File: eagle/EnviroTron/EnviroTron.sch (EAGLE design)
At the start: 14 parts

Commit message: Cleaned up small layout details
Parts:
- removed U$2: WEMOS-D1-MINI, Enviro:WEMOS-D1-MINI
- added COMMS: WEMOS-D1-MINI, EnviroTron:WEMOS-D1-MINI
- LIGHT: device Enviro:LTR-329 -> EnviroTron:LTR-329
- MOTION: device Enviro:PIR -> EnviroTron:PIR
- PRES: device Enviro:MS5607 -> EnviroTron:MS5607
- TEMP: device Enviro:SHT21 -> EnviroTron:SHT21
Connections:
- net 3V3: now also COMMS.3V3; no longer U$2.3V3
- net GND: now also COMMS.GND; no longer U$2.GND
- net PIROUT: now also COMMS.D0; no longer U$2.D0
- net SCL: now also COMMS.D1; no longer U$2.D1
- net SDA: now also COMMS.D2; no longer U$2.D2
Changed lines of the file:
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@@
 <part name="C3" library="rcl" deviceset="C-US" device="C0805" value="100n"/>
 <part name="C4" library="rcl" deviceset="C-US" device="C0805" value="100n"/>
-<part name="LIGHT" library="Enviro" deviceset="LTR-329" device=""/>
-<part name="PRES" library="Enviro" deviceset="MS5607" device=""/>
+<part name="LIGHT" library="EnviroTron" deviceset="LTR-329" device=""/>
+<part name="PRES" library="EnviroTron" deviceset="MS5607" device=""/>
 <part name="R1" library="rcl" deviceset="R-US_" device="R0805" value="10k"/>
 <part name="R2" library="rcl" deviceset="R-US_" device="R0805" value="10k"/>
 <part name="C5" library="rcl" deviceset="C-US" device="C0805" value="1u"/>
 <part name="C6" library="rcl" deviceset="C-US" device="C0805" value="10u"/>
-<part name="MOTION" library="Enviro" deviceset="PIR" device=""/>
+<part name="MOTION" library="EnviroTron" deviceset="PIR" device=""/>
 <part name="R3" library="rcl" deviceset="R-US_" device="R0805" value="10k"/>
-<part name="TEMP" library="Enviro" deviceset="SHT21" device=""/>
-<part name="U$2" library="Enviro" deviceset="WEMOS-D1-MINI" device=""/>
+<part name="TEMP" library="EnviroTron" deviceset="SHT21" device=""/>
+<part name="COMMS" library="EnviroTron" deviceset="WEMOS-D1-MINI" device=""/>
 </parts>
 <sheets>
@@
 <instance part="R3" gate="G$1" x="88.9" y="99.06"/>
 <instance part="TEMP" gate="G$1" x="68.58" y="25.4"/>
-<instance part="U$2" gate="G$1" x="17.78" y="17.78"/>
+<instance part="COMMS" gate="G$1" x="17.78" y="17.78"/>
 </instances>
 <busses>
@@
 <wire x1="7.62" y1="22.86" x2="5.08" y2="22.86" width="0.1524" layer="91"/>
 <label x="5.08" y="22.86" size="1.524" layer="95" rot="R180" xref="yes"/>
-<pinref part="U$2" gate="G$1" pin="D2"/>
+<pinref part="COMMS" gate="G$1" pin="D2"/>
 </segment>
 <segment>
@@
 <wire x1="7.62" y1="25.4" x2="5.08" y2="25.4" width="0.1524" layer="91"/>
 <label x="5.08" y="25.4" size="1.524" layer="95" rot="R180" xref="yes"/>
-<pinref part="U$2" gate="G$1" pin="D1"/>
+<pinref part="COMMS" gate="G$1" pin="D1"/>
 </segment>
 <segment>
@@
 <wire x1="27.94" y1="22.86" x2="30.48" y2="22.86" width="0.1524" layer="91"/>
 <label x="30.48" y="22.86" size="1.524" layer="95" xref="yes"/>
-<pinref part="U$2" gate="G$1" pin="3V3"/>
+<pinref part="COMMS" gate="G$1" pin="3V3"/>
 </segment>
 <segment>
@@
 <wire x1="27.94" y1="15.24" x2="30.48" y2="15.24" width="0.1524" layer="91"/>
 <label x="30.48" y="15.24" size="1.524" layer="95" xref="yes"/>
-<pinref part="U$2" gate="G$1" pin="GND"/>
+<pinref part="COMMS" gate="G$1" pin="GND"/>
 </segment>
 <segment>
@@
 <wire x1="7.62" y1="27.94" x2="5.08" y2="27.94" width="0.1524" layer="91"/>
 <label x="5.08" y="27.94" size="1.524" layer="95" rot="R180" xref="yes"/>
-<pinref part="U$2" gate="G$1" pin="D0"/>
-</segment>
-</net>
+<pinref part="COMMS" gate="G$1" pin="D0"/>
+</segment>
+</net>

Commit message: Fixed floating CSB pin on MS5607 chip
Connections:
- net GND: now also PRES.CSB
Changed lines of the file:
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@@
 <label x="96.52" y="99.06" size="1.524" layer="95" xref="yes"/>
+</segment>
+<segment>
+<pinref part="PRES" gate="G$1" pin="CSB"/>
+<wire x1="81.28" y1="78.74" x2="83.82" y2="78.74" width="0.1524" layer="91"/>
+<label x="83.82" y="78.74" size="1.524" layer="95" xref="yes"/>
 </segment>
 </net>

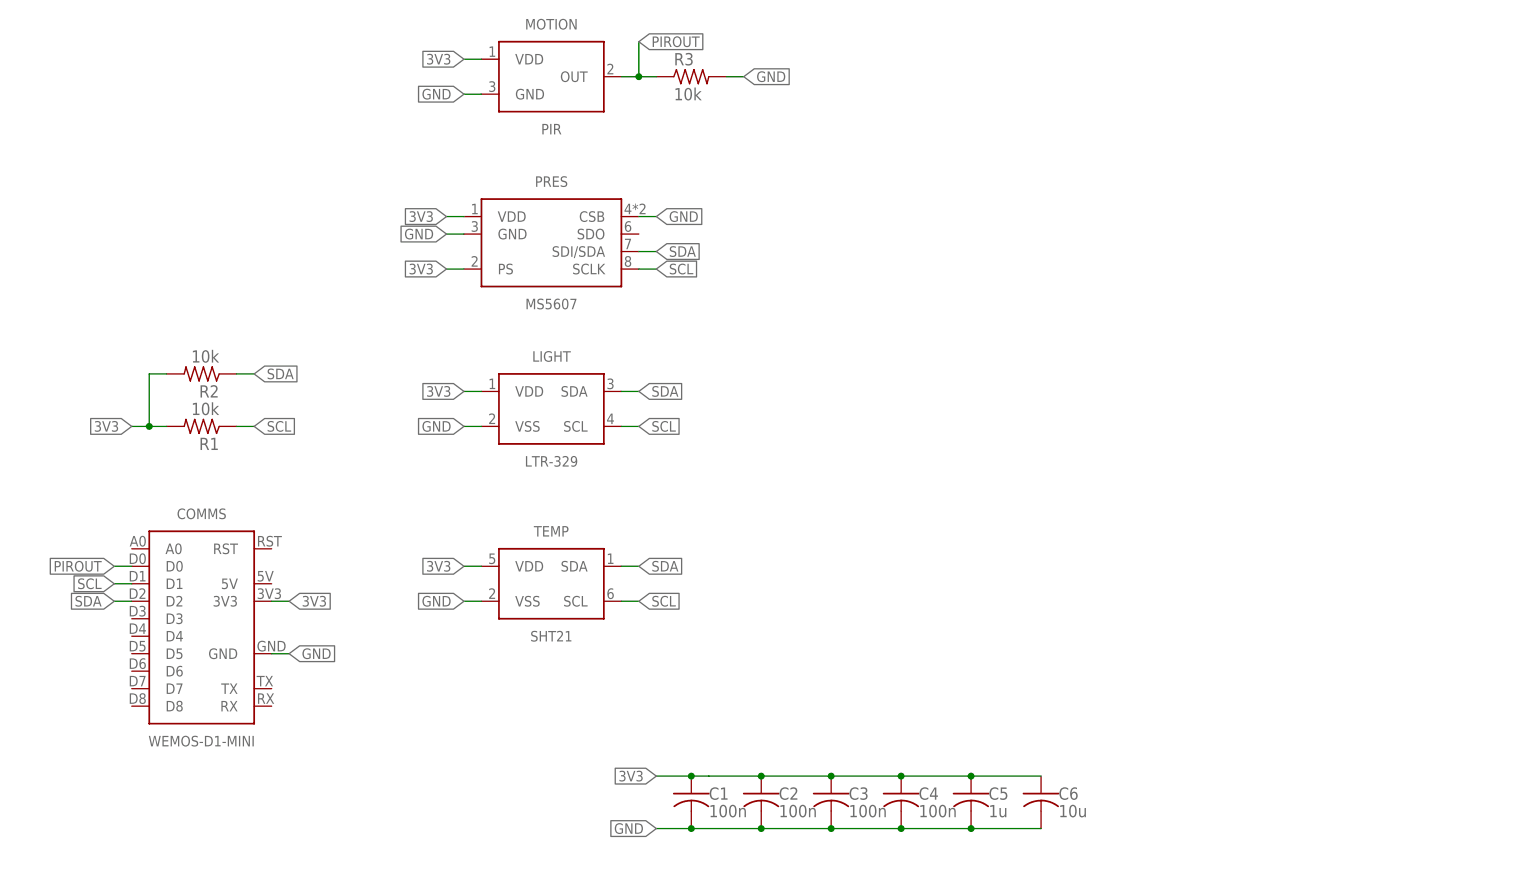
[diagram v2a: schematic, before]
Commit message: Added sound sensor to EnviroTron board. Swapped to better Pressure sensor.
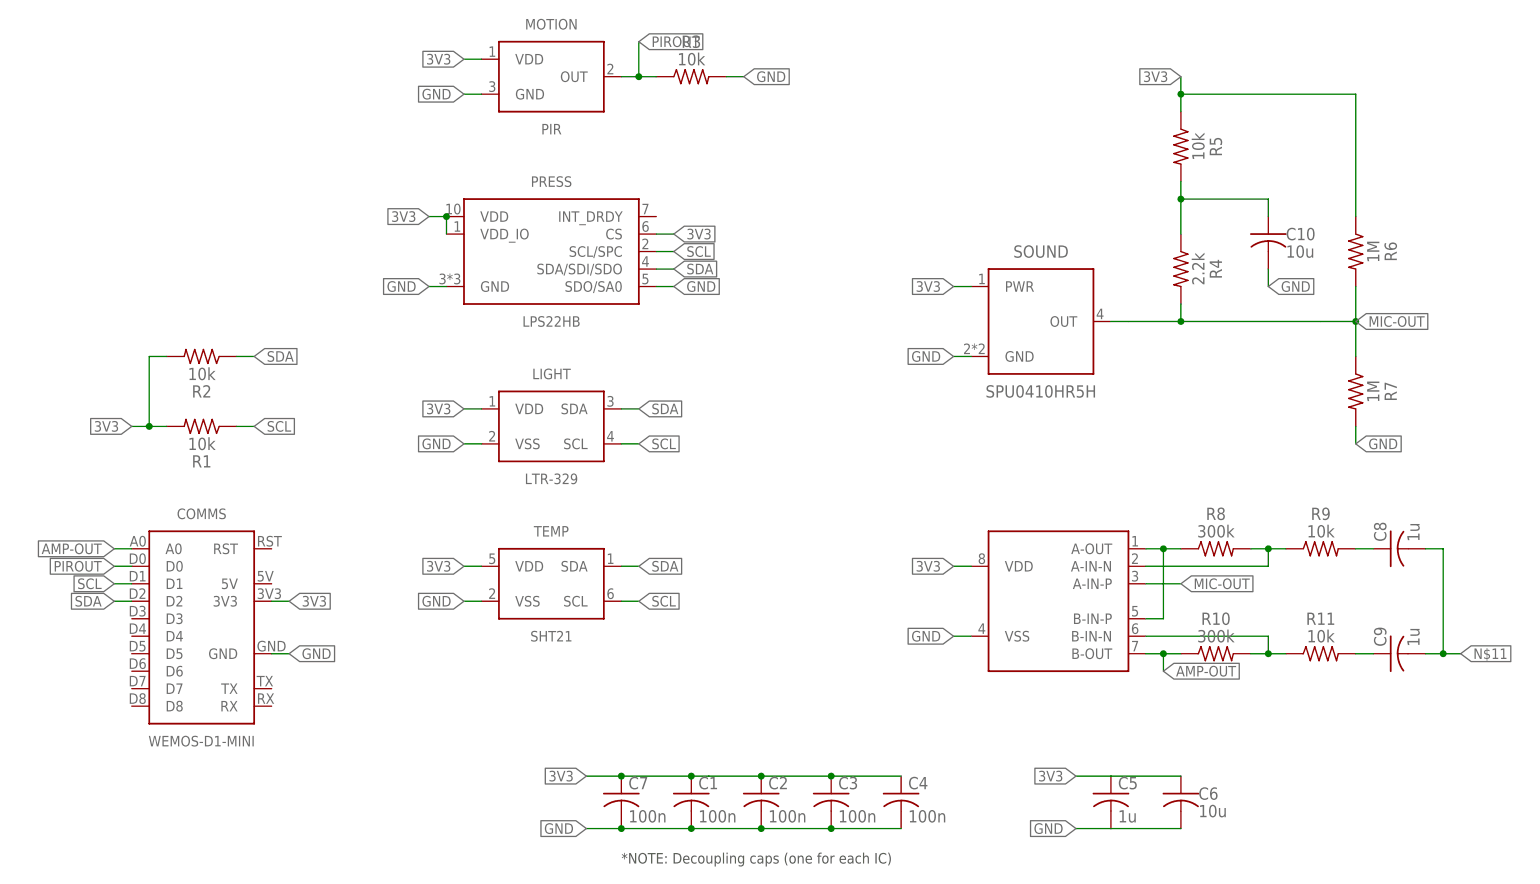
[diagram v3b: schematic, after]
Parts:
- removed PRES: MS5607, EnviroTron:MS5607
- added C10: 10u, rcl:C-USC0805
- added C7: 100n, SmslsTron-1:C-USC0603
- added C8, C9: 1u, SmslsTron-1:C-USC0603
- added PRESS: LPS22HB, EnviroTron:LPS22HB
- added R10, R8: 300k, SmslsTron-1:R-US_R0603
- added R11, R5, R9: 10k, SmslsTron-1:R-US_R0603
- added R4: 2.2k, SmslsTron-1:R-US_R0603
- added R6, R7: 1M, SmslsTron-1:R-US_R0603
- added SOUND: SPU0410HR5H, EnviroTron:SPU0410HR5H
- added U$1: MCP6002, EnviroTron:MCP6002
- C1, C2, C3, C4, C5: device rcl:C-USC0805 -> SmslsTron-1:C-USC0603
- R1, R2, R3: device rcl:R-US_R0805 -> SmslsTron-1:R-US_R0603
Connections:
- new net AMP-OUT: COMMS.A0, R10.1, U$1.B-OUT
- new net MIC-OUT: R4.2, R6.2, R7.1, SOUND.OUT, U$1.A-IN-P
- new net N$10: C9.1, R11.2
- new net N$11: C8.2, C9.2
- new net N$2: R8.1, U$1.A-OUT, U$1.B-IN-P
- new net N$3: C5.1, C6.1
- new net N$4: C5.2, C6.2
- new net N$5: C10.1, R4.1, R5.2
- new net N$6: R8.2, R9.1, U$1.A-IN-N
- new net N$7: C8.1, R9.2
- new net N$9: R10.2, R11.1, U$1.B-IN-N
- net 3V3: now also C7.1, PRESS.CS, PRESS.VDD, PRESS.VDD_IO, R5.1, R6.1, SOUND.PWR; no longer C5.1, C6.1, PRES.PS, PRES.VDD
- net GND: now also C10.2, C7.2, PRESS.GND, PRESS.SDO/SA0, R7.2, SOUND.GND; no longer C5.2, C6.2, PRES.CSB, PRES.GND
- net SCL: now also PRESS.SCL/SPC; no longer PRES.SCLK
- net SDA: now also PRESS.SDA/SDI/SDO; no longer PRES.SDI/SDA
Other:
- note added: "*NOTE: Decoupling caps (one for each IC)"
- moved on the sheet: C6, LIGHT, R2

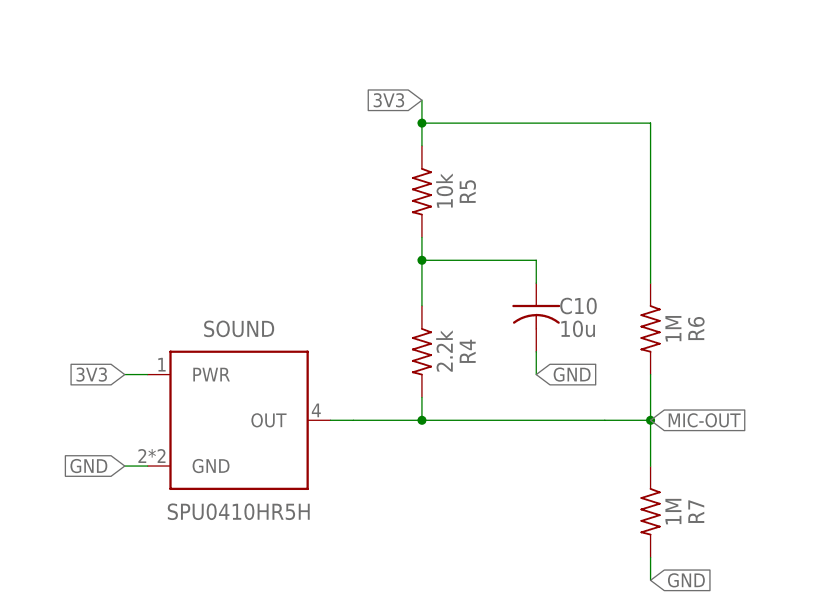
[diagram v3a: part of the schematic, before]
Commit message: Added DC blocking cap to mic pre-amp circuit.
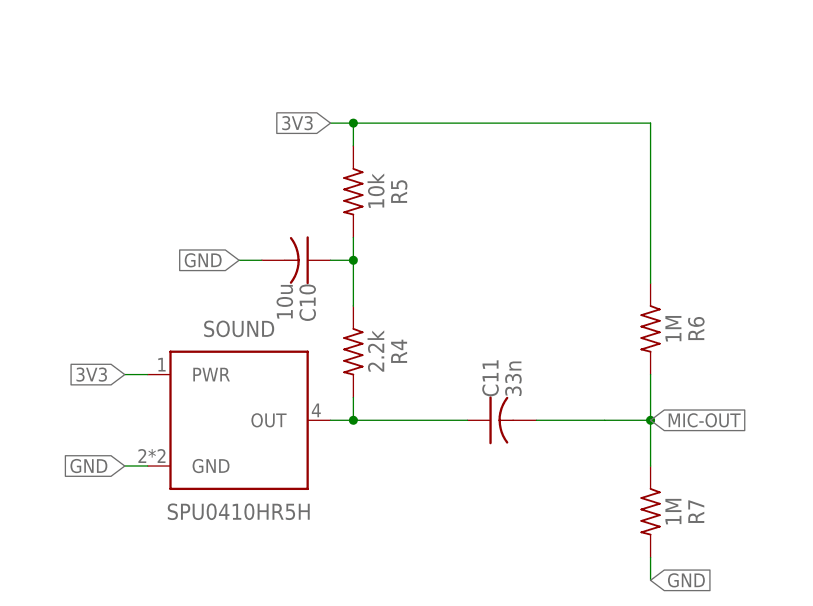
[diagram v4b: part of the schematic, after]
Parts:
- added C11: 33n, rcl:C-USC0805
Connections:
- new net N$8: C11.1, R4.2, SOUND.OUT
- net MIC-OUT: now also C11.2; no longer R4.2, SOUND.OUT
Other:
- moved on the sheet: C10, R4, R5
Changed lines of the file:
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@@
 <part name="R10" library="SmslsTron-1" deviceset="R-US_" device="R0603" value="300k"/>
 <part name="R11" library="SmslsTron-1" deviceset="R-US_" device="R0603" value="10k"/>
+<part name="C11" library="rcl" deviceset="C-US" device="C0805" value="33n"/>
 </parts>
 <sheets>
@@
 <instance part="C8" gate="G$1" x="190.5" y="30.48" rot="R90"/>
 <instance part="C9" gate="G$1" x="190.5" y="15.24" rot="R90"/>
-<instance part="R4" gate="G$1" x="160.02" y="71.12" rot="R270"/>
-<instance part="R5" gate="G$1" x="160.02" y="88.9" rot="R270"/>
-<instance part="C10" gate="G$1" x="172.72" y="76.2"/>
+<instance part="R4" gate="G$1" x="152.4" y="71.12" rot="R270"/>
+<instance part="R5" gate="G$1" x="152.4" y="88.9" rot="R270"/>
+<instance part="C10" gate="G$1" x="147.32" y="81.28" rot="R270"/>
 <instance part="R6" gate="G$1" x="185.42" y="73.66" rot="R270"/>
 <instance part="R7" gate="G$1" x="185.42" y="53.34" rot="R270"/>
@@
 <instance part="R10" gate="G$1" x="165.1" y="15.24"/>
 <instance part="R11" gate="G$1" x="180.34" y="15.24"/>
+<instance part="C11" gate="G$1" x="167.64" y="63.5" rot="R90"/>
 </instances>
 <busses>
@@
 <segment>
 <pinref part="R5" gate="G$1" pin="1"/>
-<wire x1="160.02" y1="93.98" x2="160.02" y2="96.52" width="0.1524" layer="91"/>
+<wire x1="152.4" y1="93.98" x2="152.4" y2="96.52" width="0.1524" layer="91"/>
 <pinref part="R6" gate="G$1" pin="1"/>
-<wire x1="160.02" y1="96.52" x2="185.42" y2="96.52" width="0.1524" layer="91"/>
+<wire x1="152.4" y1="96.52" x2="185.42" y2="96.52" width="0.1524" layer="91"/>
 <wire x1="185.42" y1="96.52" x2="185.42" y2="78.74" width="0.1524" layer="91"/>
-<wire x1="160.02" y1="96.52" x2="160.02" y2="99.06" width="0.1524" layer="91"/>
-<junction x="160.02" y="96.52"/>
-<label x="160.02" y="99.06" size="1.524" layer="95" rot="R180" xref="yes"/>
+<wire x1="152.4" y1="96.52" x2="149.86" y2="96.52" width="0.1524" layer="91"/>
+<junction x="152.4" y="96.52"/>
+<label x="149.86" y="96.52" size="1.524" layer="95" rot="R180" xref="yes"/>
 </segment>
 </net>
@@
 <segment>
 <pinref part="C10" gate="G$1" pin="2"/>
-<wire x1="172.72" y1="71.12" x2="172.72" y2="68.58" width="0.1524" layer="91"/>
-<label x="172.72" y="68.58" size="1.524" layer="95" xref="yes"/>
+<wire x1="142.24" y1="81.28" x2="139.7" y2="81.28" width="0.1524" layer="91"/>
+<label x="139.7" y="81.28" size="1.524" layer="95" rot="R180" xref="yes"/>
 </segment>
 <segment>
@@
 <net name="MIC-OUT" class="0">
 <segment>
-<pinref part="SOUND" gate="G$1" pin="OUT"/>
-<wire x1="149.86" y1="63.5" x2="152.4" y2="63.5" width="0.1524" layer="91"/>
-<pinref part="R4" gate="G$1" pin="2"/>
-<wire x1="152.4" y1="63.5" x2="160.02" y2="63.5" width="0.1524" layer="91"/>
-<wire x1="160.02" y1="63.5" x2="160.02" y2="66.04" width="0.1524" layer="91"/>
-<wire x1="160.02" y1="63.5" x2="180.34" y2="63.5" width="0.1524" layer="91"/>
-<junction x="160.02" y="63.5"/>
 <pinref part="R6" gate="G$1" pin="2"/>
 <wire x1="180.34" y1="63.5" x2="185.42" y2="63.5" width="0.1524" layer="91"/>
@@
 <junction x="185.42" y="63.5"/>
 <label x="185.42" y="63.5" size="1.524" layer="95" xref="yes"/>
+<pinref part="C11" gate="G$1" pin="2"/>
+<wire x1="172.72" y1="63.5" x2="180.34" y2="63.5" width="0.1524" layer="91"/>
 </segment>
 <segment>
@@
 <pinref part="R4" gate="G$1" pin="1"/>
 <pinref part="R5" gate="G$1" pin="2"/>
-<wire x1="160.02" y1="76.2" x2="160.02" y2="81.28" width="0.1524" layer="91"/>
+<wire x1="152.4" y1="76.2" x2="152.4" y2="81.28" width="0.1524" layer="91"/>
 <pinref part="C10" gate="G$1" pin="1"/>
-<wire x1="160.02" y1="81.28" x2="160.02" y2="83.82" width="0.1524" layer="91"/>
-<wire x1="172.72" y1="78.74" x2="172.72" y2="81.28" width="0.1524" layer="91"/>
-<wire x1="172.72" y1="81.28" x2="160.02" y2="81.28" width="0.1524" layer="91"/>
-<junction x="160.02" y="81.28"/>
+<wire x1="152.4" y1="81.28" x2="152.4" y2="83.82" width="0.1524" layer="91"/>
+<wire x1="149.86" y1="81.28" x2="152.4" y2="81.28" width="0.1524" layer="91"/>
+<junction x="152.4" y="81.28"/>
 </segment>
 </net>
@@
 </segment>
 </net>
+<net name="N$8" class="0">
+<segment>
+<pinref part="R4" gate="G$1" pin="2"/>
+<wire x1="152.4" y1="63.5" x2="152.4" y2="66.04" width="0.1524" layer="91"/>
+<pinref part="SOUND" gate="G$1" pin="OUT"/>
+<wire x1="149.86" y1="63.5" x2="152.4" y2="63.5" width="0.1524" layer="91"/>
+<pinref part="C11" gate="G$1" pin="1"/>
+<wire x1="152.4" y1="63.5" x2="165.1" y2="63.5" width="0.1524" layer="91"/>
+<junction x="152.4" y="63.5"/>
+</segment>
+</net>

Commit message: Completed initial routing of all signals for new board layout.
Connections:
- removed net N$11: C8.2, C9.2
- removed net N$3: C5.1, C6.1
- removed net N$4: C5.2, C6.2
- net 3V3: now also C5.1, C6.1, U$1.VDD
- net GND: now also C5.2, C6.2, C8.2, C9.2, U$1.VSS
- net PIROUT: now also COMMS.D8; no longer COMMS.D0
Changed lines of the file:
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@@
 <wire x1="129.54" y1="27.94" x2="127" y2="27.94" width="0.1524" layer="91"/>
 <label x="127" y="27.94" size="1.524" layer="95" rot="R180" xref="yes"/>
+<pinref part="U$1" gate="G$1" pin="VDD"/>
 </segment>
 <segment>
 <wire x1="149.86" y1="-2.54" x2="144.78" y2="-2.54" width="0.1524" layer="91"/>
 <label x="144.78" y="-2.54" size="1.524" layer="95" rot="R180" xref="yes"/>
+<pinref part="C6" gate="G$1" pin="1"/>
+<pinref part="C5" gate="G$1" pin="1"/>
+<wire x1="149.86" y1="-2.54" x2="160.02" y2="-2.54" width="0.1524" layer="91"/>
+<junction x="149.86" y="-2.54"/>
 </segment>
 <segment>
@@
 <wire x1="129.54" y1="17.78" x2="127" y2="17.78" width="0.1524" layer="91"/>
 <label x="127" y="17.78" size="1.524" layer="95" rot="R180" xref="yes"/>
+<pinref part="U$1" gate="G$1" pin="VSS"/>
 </segment>
 <segment>
 <wire x1="149.86" y1="-10.16" x2="144.78" y2="-10.16" width="0.1524" layer="91"/>
 <label x="144.78" y="-10.16" size="1.524" layer="95" rot="R180" xref="yes"/>
+<pinref part="C6" gate="G$1" pin="2"/>
+<pinref part="C5" gate="G$1" pin="2"/>
+<wire x1="149.86" y1="-10.16" x2="160.02" y2="-10.16" width="0.1524" layer="91"/>
+<junction x="149.86" y="-10.16"/>
 </segment>
 <segment>
@@
 <wire x1="185.42" y1="48.26" x2="185.42" y2="45.72" width="0.1524" layer="91"/>
 <label x="185.42" y="45.72" size="1.524" layer="95" xref="yes"/>
+</segment>
+<segment>
+<pinref part="C8" gate="G$1" pin="2"/>
+<wire x1="195.58" y1="30.48" x2="198.12" y2="30.48" width="0.1524" layer="91"/>
+<wire x1="198.12" y1="30.48" x2="198.12" y2="15.24" width="0.1524" layer="91"/>
+<pinref part="C9" gate="G$1" pin="2"/>
+<wire x1="198.12" y1="15.24" x2="195.58" y2="15.24" width="0.1524" layer="91"/>
+<wire x1="198.12" y1="15.24" x2="200.66" y2="15.24" width="0.1524" layer="91"/>
+<junction x="198.12" y="15.24"/>
+<label x="200.66" y="15.24" size="1.524" layer="95" xref="yes"/>
 </segment>
 </net>
@@
 </segment>
 <segment>
-<wire x1="7.62" y1="27.94" x2="5.08" y2="27.94" width="0.1524" layer="91"/>
-<label x="5.08" y="27.94" size="1.524" layer="95" rot="R180" xref="yes"/>
-<pinref part="COMMS" gate="G$1" pin="D0"/>
+<label x="5.08" y="7.62" size="1.524" layer="95" rot="R180" xref="yes"/>
+<wire x1="5.08" y1="7.62" x2="7.62" y2="7.62" width="0.1524" layer="91"/>
+<pinref part="COMMS" gate="G$1" pin="D8"/>
 </segment>
 </net>
@@
 </segment>
 </net>
-<net name="N$3" class="0">
-<segment>
-<pinref part="C6" gate="G$1" pin="1"/>
-<pinref part="C5" gate="G$1" pin="1"/>
-<wire x1="149.86" y1="-2.54" x2="160.02" y2="-2.54" width="0.1524" layer="91"/>
-</segment>
-</net>
-<net name="N$4" class="0">
-<segment>
-<pinref part="C6" gate="G$1" pin="2"/>
-<pinref part="C5" gate="G$1" pin="2"/>
-<wire x1="149.86" y1="-10.16" x2="160.02" y2="-10.16" width="0.1524" layer="91"/>
-</segment>
-</net>
 <net name="N$5" class="0">
 <segment>
@@
 </segment>
 </net>
-<net name="N$11" class="0">
-<segment>
-<pinref part="C8" gate="G$1" pin="2"/>
-<wire x1="195.58" y1="30.48" x2="198.12" y2="30.48" width="0.1524" layer="91"/>
-<wire x1="198.12" y1="30.48" x2="198.12" y2="15.24" width="0.1524" layer="91"/>
-<pinref part="C9" gate="G$1" pin="2"/>
-<wire x1="198.12" y1="15.24" x2="195.58" y2="15.24" width="0.1524" layer="91"/>
-<wire x1="198.12" y1="15.24" x2="200.66" y2="15.24" width="0.1524" layer="91"/>
-<junction x="198.12" y="15.24"/>
-<label x="200.66" y="15.24" size="1.524" layer="95" xref="yes"/>
-</segment>
-</net>
